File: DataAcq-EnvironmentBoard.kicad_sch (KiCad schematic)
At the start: 31 parts, among them J2 CAN Output, J3 CAN Input, U1 SHT45, U2 FS3000-1005, U3 LMT87DCK, U4 Daughterboard Connector

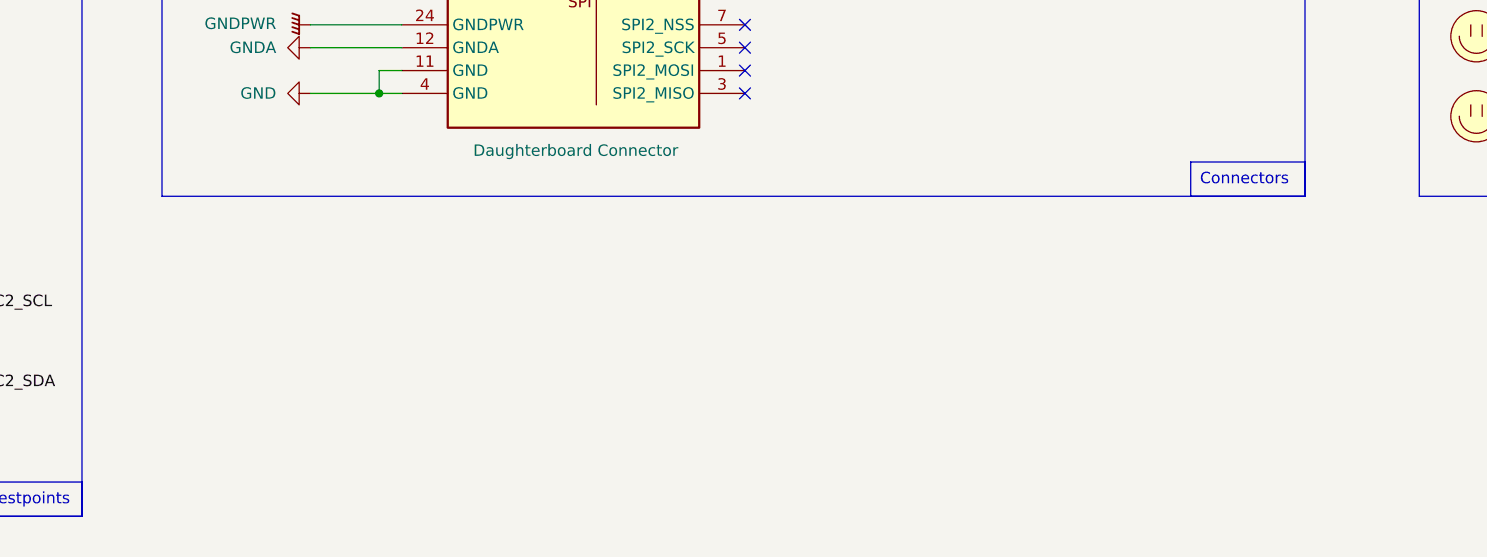
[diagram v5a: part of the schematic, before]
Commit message: add breakout board connectors to sch
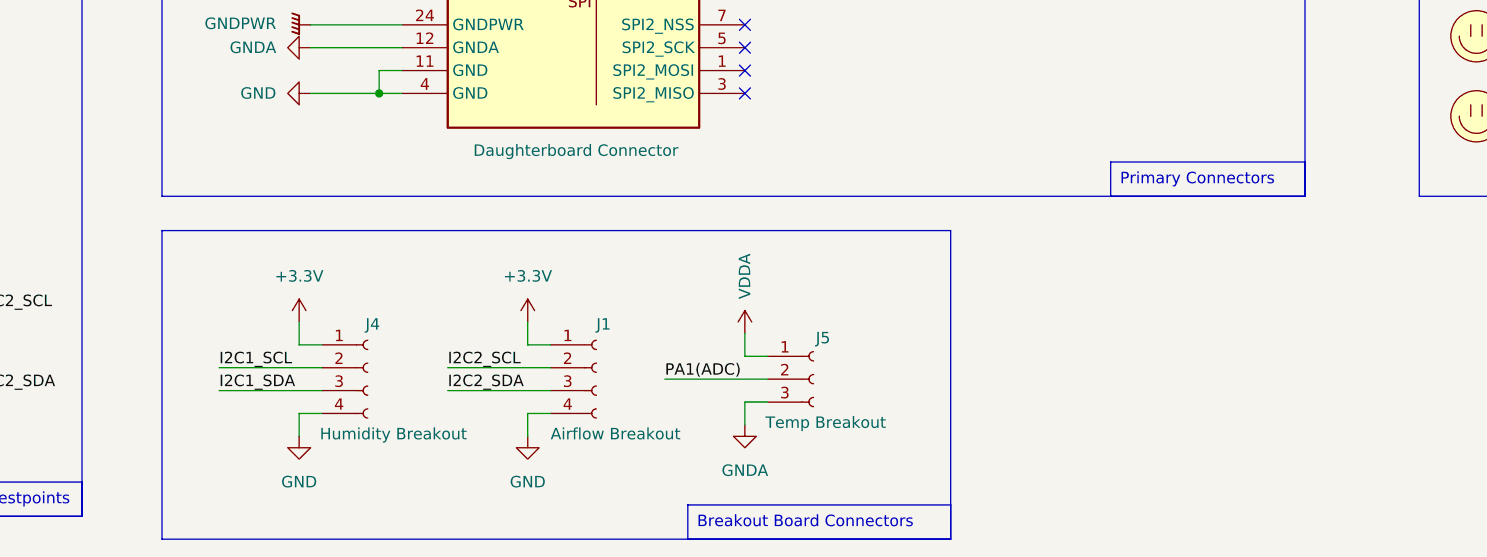
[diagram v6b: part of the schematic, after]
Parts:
- added J1: Airflow Breakout, symbol Connector:Conn_01x04_Socket
- added J4: Humidity Breakout, symbol Connector:Conn_01x04_Socket
- added J5: Temp Breakout, symbol Connector:Conn_01x03_Socket
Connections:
- net +3.3V: now also J1.1 (Pin_1), J4.1 (Pin_1)
- net GND: now also J1.4 (Pin_4), J4.4 (Pin_4)
- net GNDA: now also J5.3 (Pin_3)
- net I2C1_SCL: now also J4.2 (Pin_2)
- net I2C1_SDA: now also J4.3 (Pin_3)
- net I2C2_SCL: now also J1.2 (Pin_2)
- net I2C2_SDA: now also J1.3 (Pin_3)
- net PA1(ADC): now also J5.2 (Pin_2)
- net VDDA: now also J5.1 (Pin_1)

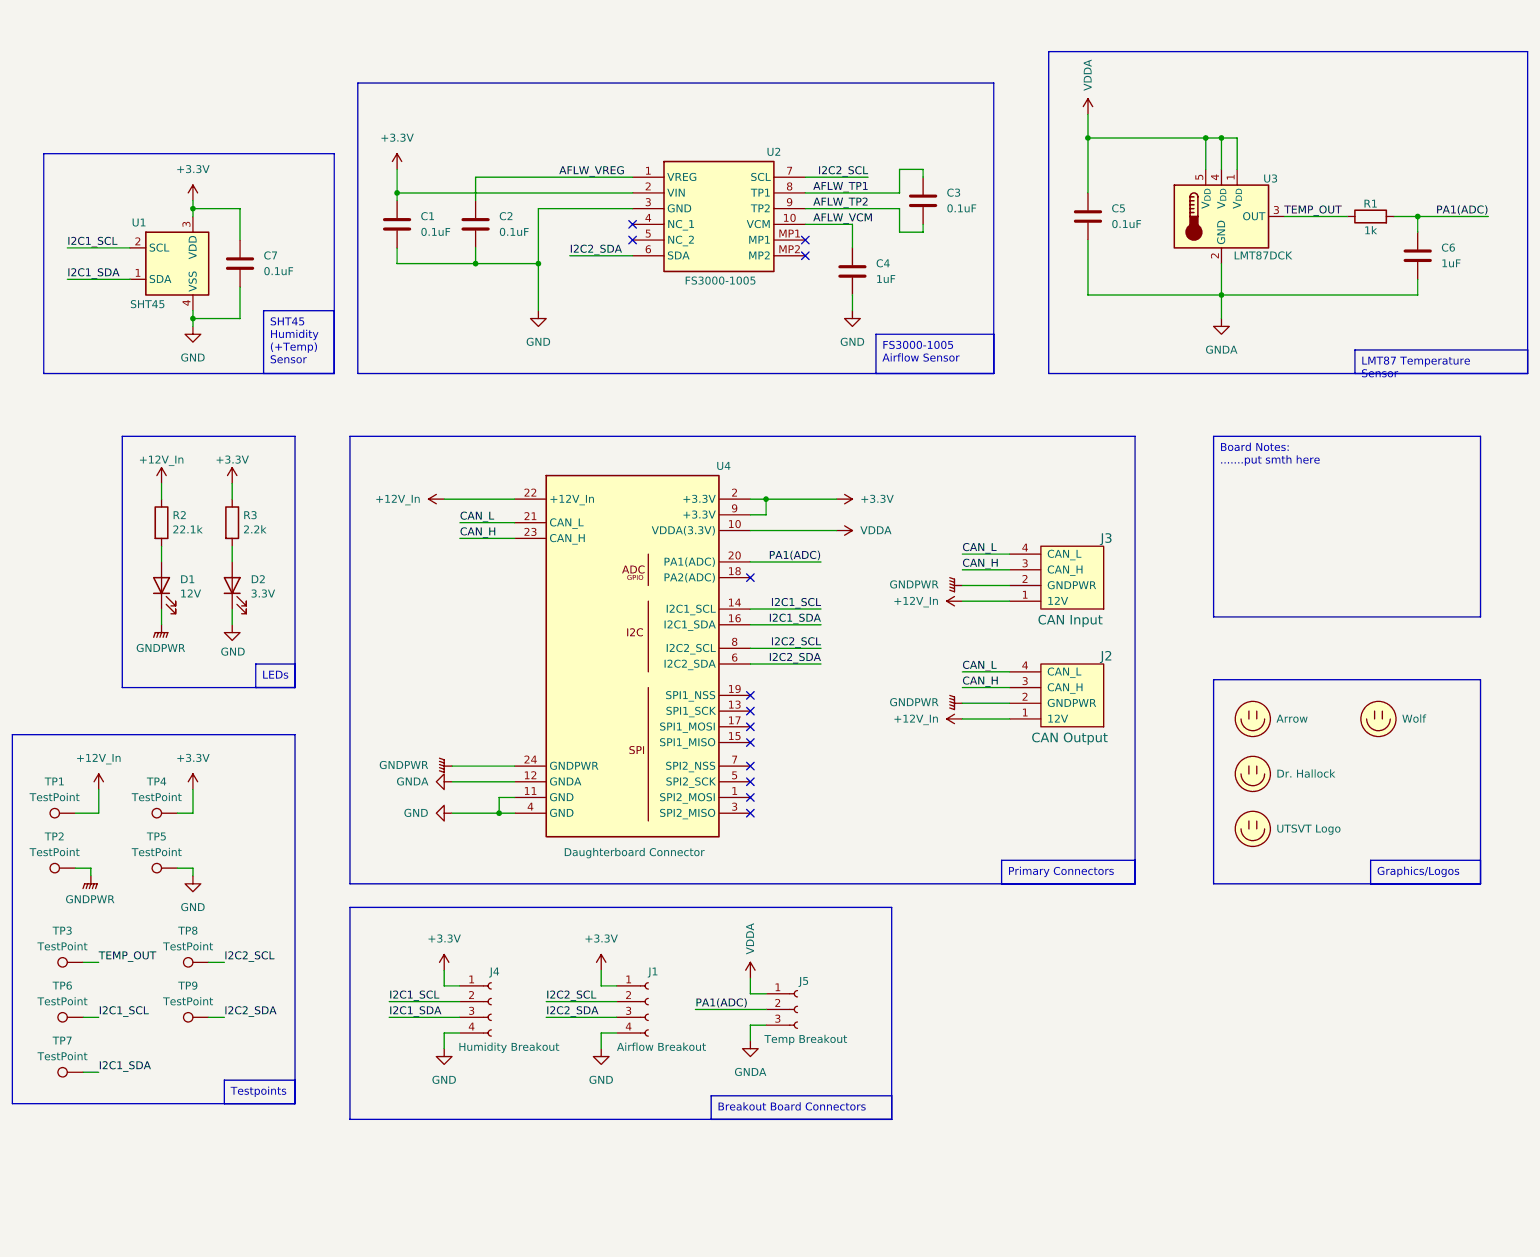
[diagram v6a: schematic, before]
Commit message: add TVS diodes and fuses for breakout
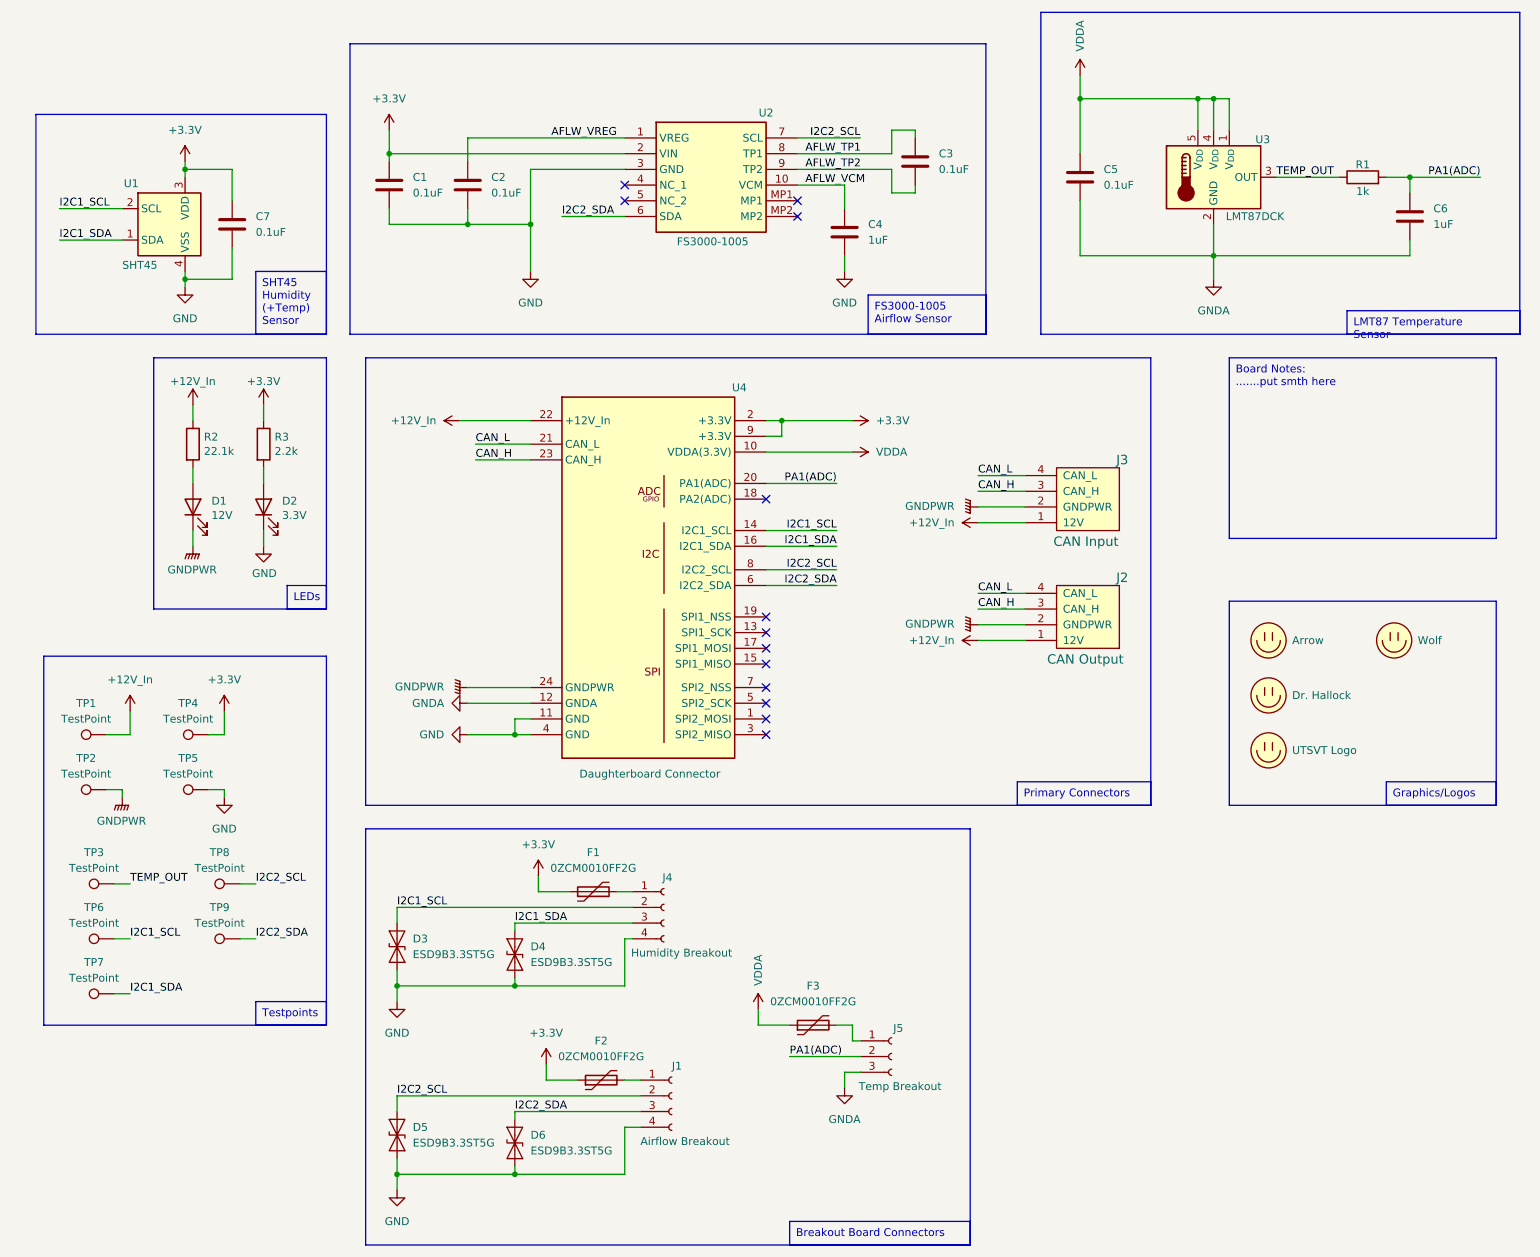
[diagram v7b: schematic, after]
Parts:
- added D3, D4, D5, D6: ESD9B3.3ST5G, Diode_SMD:D_SOD-923, symbol Diode:ESD9B3.3ST5G
- added F1, F2, F3: 0ZCM0010FF2G, symbol Device:Polyfuse
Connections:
- net +3.3V: now also F1.1, F2.1; no longer J1.1 (Pin_1), J4.1 (Pin_1)
- net GND: now also D3.2 (A2), D4.2 (A2), D5.2 (A2), D6.2 (A2)
- net I2C1_SCL: now also D3.1 (A1)
- net I2C1_SDA: now also D4.1 (A1)
- net I2C2_SCL: now also D5.1 (A1)
- net I2C2_SDA: now also D6.1 (A1)
- net VDDA: now also F3.1; no longer J5.1 (Pin_1)
- new net: F3.2, J5.1 (Pin_1)
- new net: F2.2, J1.1 (Pin_1)
- new net: F1.2, J4.1 (Pin_1)
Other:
- moved on the sheet: C1, C2, C3, C4, C5, C6, C7, D1, D2, J1, J2, J3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

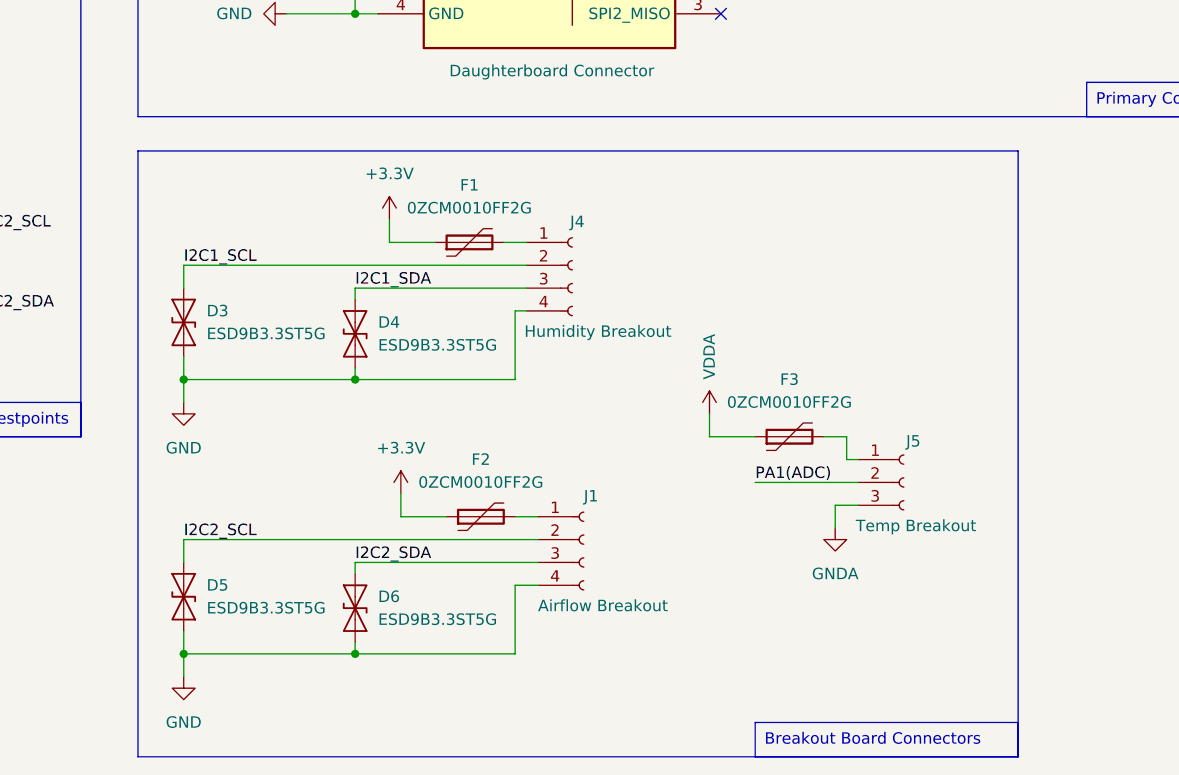
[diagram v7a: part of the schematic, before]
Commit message: assign footprints and PN
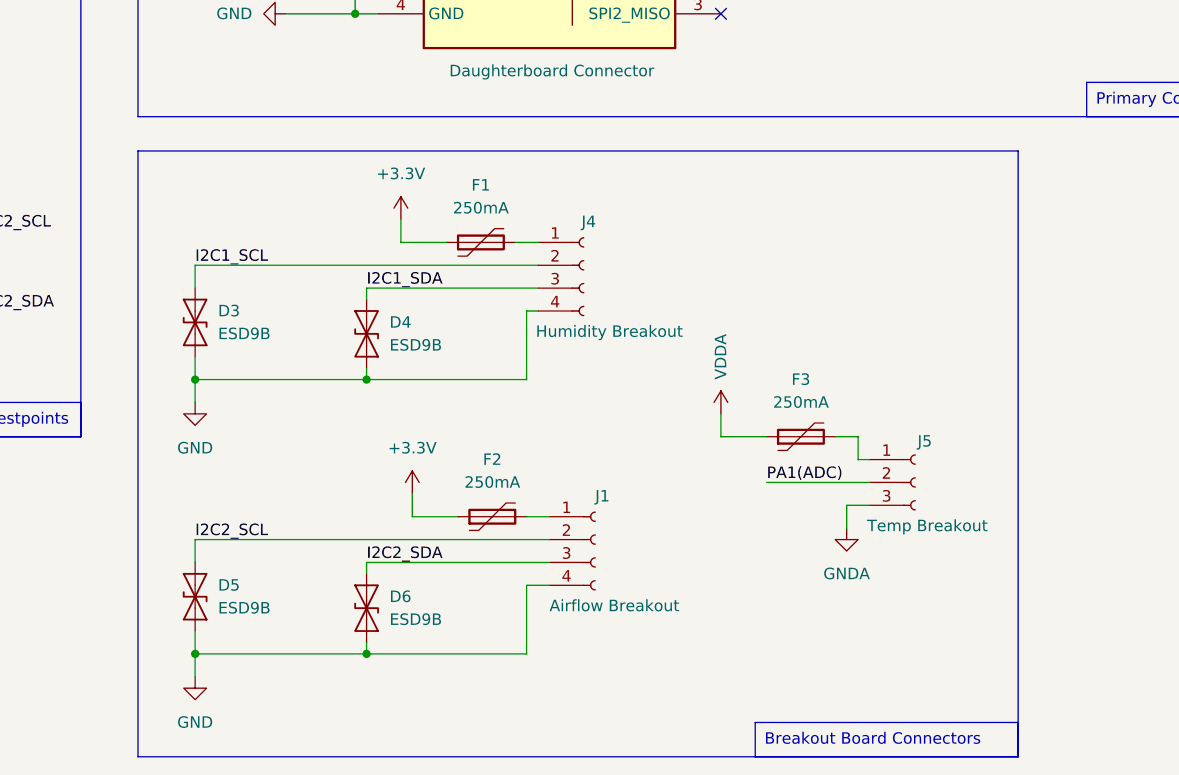
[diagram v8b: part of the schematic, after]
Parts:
- D3, D4, D5, D6: value ESD9B3.3ST5G -> ESD9B; P/N (none) -> ESD9B3.3ST5G
- F1, F2, F3: value 0ZCM0010FF2G -> 250mA; footprint (none) -> Fuse:Fuse_0603_1608Metric; P/N (none) -> 0ZCM0010FF2G
- J1: footprint (none) -> UTSVT_Connectors:Molex_MicroFit3.0_1x4xP3.00mm_PolarizingPeg_Vertical; P/N (none) -> (none)
- J4: footprint (none) -> UTSVT_Connectors:Molex_MicroFit3.0_1x4xP3.00mm_PolarizingPeg_Vertical
- J5: footprint (none) -> UTSVT_Connectors:Molex_MicroFit3.0_1x3xP3.00mm_PolarizingPeg_Vertical
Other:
- moved on the sheet: D3, D4, D5, D6, F1, F2, F3, J1, J4, J5
